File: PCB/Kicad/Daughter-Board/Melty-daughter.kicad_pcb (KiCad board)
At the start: 2 copper layers, 30 x 20 mm, 9 parts, among them J1 Conn_01x07_Female, Q1 SFH 325

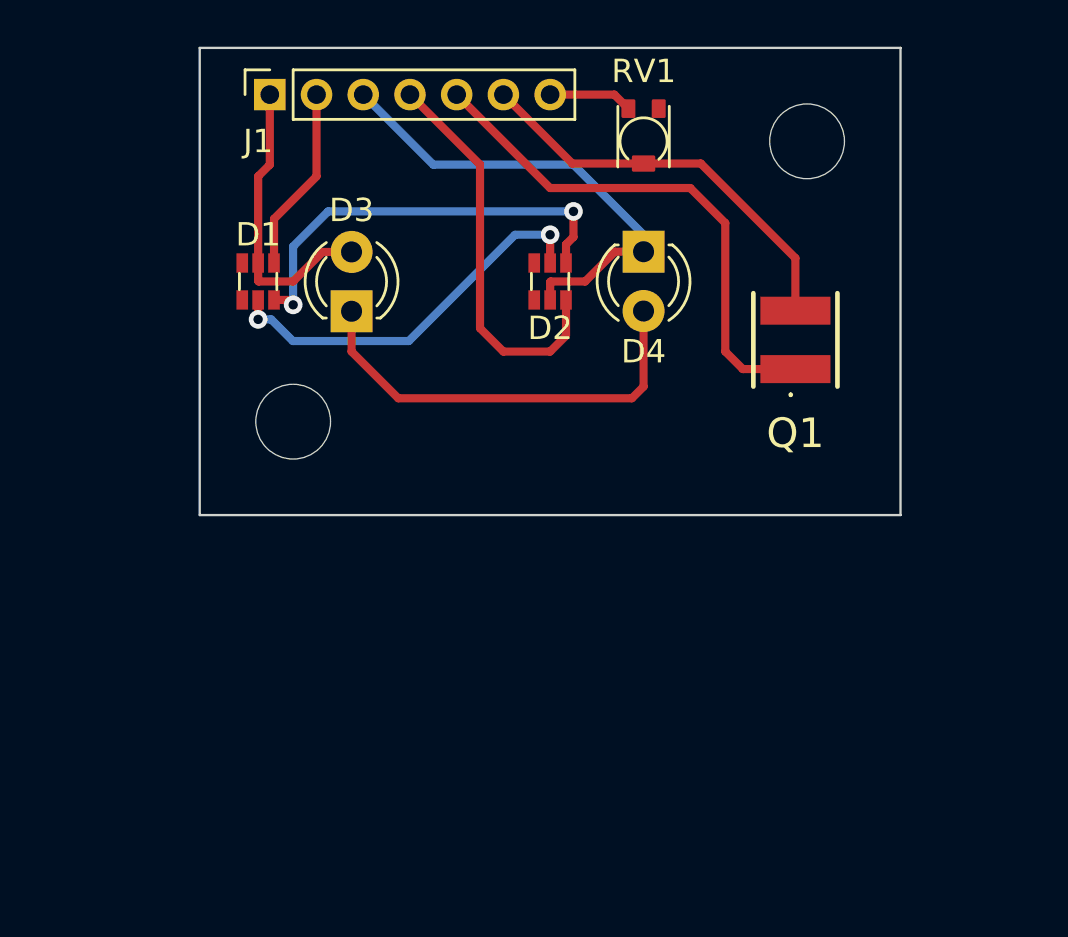
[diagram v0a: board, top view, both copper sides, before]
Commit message: Add IR Board schematic and PCB design
Add kicad files for the schematic and PCB of the IR Board.
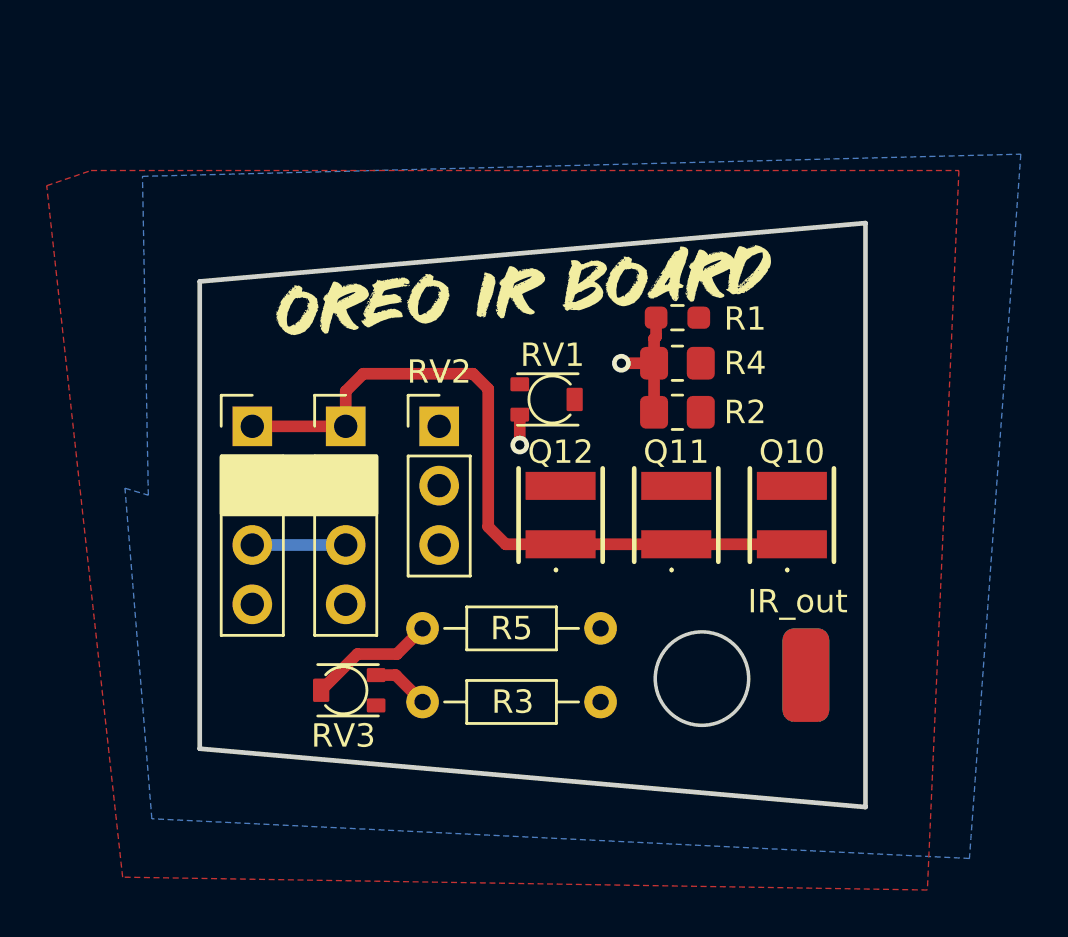
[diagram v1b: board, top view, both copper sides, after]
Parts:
- removed D1, D2: LED_RGB, KiCad:LED_RGB_Harvatek_B3803FCH
- removed D3, D4: LED, LED_THT:LED_D3.0mm
- removed Q1: SFH 325, KiCad:SFH325FA34Z
- removed the REF** at (104.0, 86.0)
- removed the REF** at (126.0, 74.0)
- added G***: LOGO, LOGO, F.Cu at (113.9, 80.4)
- added G***: LOGO, LOGO, B.Cu at (114.0, 80.4)
- added J2: Conn_01x04_Female, Connector_PinHeader_2.54mm:PinHeader_1x04_P2.54mm_Vertical, F.Cu at (106.2, 86.2)
- added P1, P2: SolderWirePad_1x01_SMD_1x2mm, Connector_Wire:SolderWirePad_1x01_SMD_1x2mm, F.Cu at (126.0, 96.8)
- added Q10: SFH 325, KiCad:SFH325FA34Z, F.Cu at (125.3, 90.0)
- added Q11: SFH 325, KiCad:SFH325FA34Z, F.Cu at (120.4, 90.0)
- added Q12: SFH 325, KiCad:SFH325FA34Z, F.Cu at (115.5, 90.0)
- added R1: R, Resistor_SMD:R_0603_1608Metric_Pad0.98x0.95mm_HandSolder, F.Cu at (120.5, 81.5)
- added R2: R_Small, Resistor_SMD:R_0805_2012Metric_Pad1.20x1.40mm_HandSolder, F.Cu at (120.5, 85.6)
- added R3: R_Small, Resistor_THT:R_Axial_DIN0204_L3.6mm_D1.6mm_P7.62mm_Horizontal, F.Cu at (117.2, 98.0)
- added R4: R_Small, Resistor_SMD:R_0805_2012Metric_Pad1.20x1.40mm_HandSolder, F.Cu at (120.5, 83.5)
- added R5: R_Small, Resistor_THT:R_Axial_DIN0204_L3.6mm_D1.6mm_P7.62mm_Horizontal, F.Cu at (117.2, 94.8)
- added REF**: OSHW-Logo2_9.8x8mm_SilkScreen, Symbol:OSHW-Logo2_9.8x8mm_SilkScreen, B.Cu at (123.2, 86.4)
- added RV2: 1K, Connector_PinHeader_2.54mm:PinHeader_1x03_P2.54mm_Vertical, F.Cu at (110.2, 86.2)
- added RV3: 1K, KiCad:Potentiometer_Bourns_TC42_Horizontal, F.Cu at (106.2, 97.5)
- J1: value Conn_01x07_Female -> Conn_01x04_Female; footprint Connector_PinSocket_2.00mm:PinSocket_1x07_P2.00mm_Vertical -> Connector_PinHeader_2.54mm:PinHeader_1x04_P2.54mm_Vertical
- moved J1 14.2 mm to (102.2, 86.2), turned to 0 degrees
- moved RV1 11.7 mm to (115.1, 85.0), turned to -90 degrees
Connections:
- J1 pad 1: Net-(D1-Pad6) -> +3V3
- J1 pad 2: Net-(D1-Pad5) -> IR_out
- J1 pad 4: Net-(D2-Pad2) -> GND
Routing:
- net Net-(D3-Pad1): track 18.5 -> 0.00 mm
- net Net-(D1-Pad2): track 18.4 -> 0.00 mm, vias 2 -> 0
- net Net-(D2-Pad2): track 17.1 -> 0.00 mm
- net Net-(D1-Pad1): track 16.8 -> 0.00 mm, vias 2 -> 0
- net Net-(J2-Pad3): track 20.5 -> 4.00 mm
- net IR_out: track 17.6 -> 4.00 mm
- net Net-(D1-Pad6): track 12.7 -> 0.00 mm
- net +3V3: track 22.6 -> 31.4 mm
- net Net-(D1-Pad5): track 7.96 -> 0.00 mm
- net GND: track 3.60 -> 9.25 mm, vias 0 -> 2
- net Net-(R5-Pad2): track 0.00 -> 5.44 mm
- added copper zone on B.Cu, net GND
- added copper zone on F.Cu, net IR_out
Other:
- board size 30 x 20 mm -> 28.5 x 25 mm
- board text added: "30.07.23"
- board text added: "3V3"
- board text added: "GND"
- board text added: "IR_out"
- board text added: "JLCJLCJLCJLC"
- board text added: "V1.0"
